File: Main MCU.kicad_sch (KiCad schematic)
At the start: 15 parts, among them J9 Conn_01x06_Pin, SW3 RESET, U1 STM32F407VGTx

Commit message: Your descriptive message here
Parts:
- added R53, R54, R55, R56: 560, Resistor_SMD:R_0603_1608Metric, symbol Device:R_US
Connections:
- net B_PWM: now also U1.44 (PE13); no longer U1.66 (PC9)
- net GND: now also D10.1 (K), D11.1 (K), D12.1 (K), D9.1 (K)
- net G_PWM: now also U1.42 (PE11); no longer U1.26 (PA3)
- net R_PWM: now also U1.40 (PE9); no longer U1.45 (PE14)
- net PA0: now reaches U1.23 (PA0)
- net PA0: now also J8.9 (Pin_9)
- net PA5: now reaches U1.30 (PA5)
- net PA5: now also J8.6 (Pin_6)
- net PA6: now reaches U1.31 (PA6)
- net PA6: now also J8.8 (Pin_8)
- net PB1: now reaches U1.36 (PB1)
- net PB1: now also J8.15 (Pin_15)
- net PD11: now reaches U1.58 (PD11)
- net PD11: now also R53.2
- net PD12: now reaches U1.59 (PD12)
- net PD12: now also R54.2
- net PD13: now reaches U1.60 (PD13)
- net PD13: now also R55.1
- net PD14: now reaches U1.61 (PD14)
- net PD14: now also R56.1
- net PD15: now reaches U1.62 (PD15)
- net PD15: now also J8.17 (Pin_17)
- net PA8: now reaches U1.67 (PA8)
- net PA8: now also J8.4 (Pin_4)
- net PC11: now reaches U1.79 (PC11)
- net PC11: now also J8.18 (Pin_18)
- net PB5: now reaches U1.91 (PB5)
- net PB5: now also J8.7 (Pin_7)
- net PA3: now reaches J8.14 (Pin_14)
- net PA3: now also U1.26 (PA3)
- net PE14: now reaches J8.16 (Pin_16)
- net PE14: now also U1.45 (PE14)
- net PC9: now reaches J8.5 (Pin_5)
- net PC9: now also U1.66 (PC9)
- net at D9.2 (A): now also R54.1
- net at D11.2 (A): now also R56.2
- net at D12.2 (A): now also R53.1
- net at D10.2 (A): now also R55.2
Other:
- moved on the sheet: D10, D11, D12, D9, J8

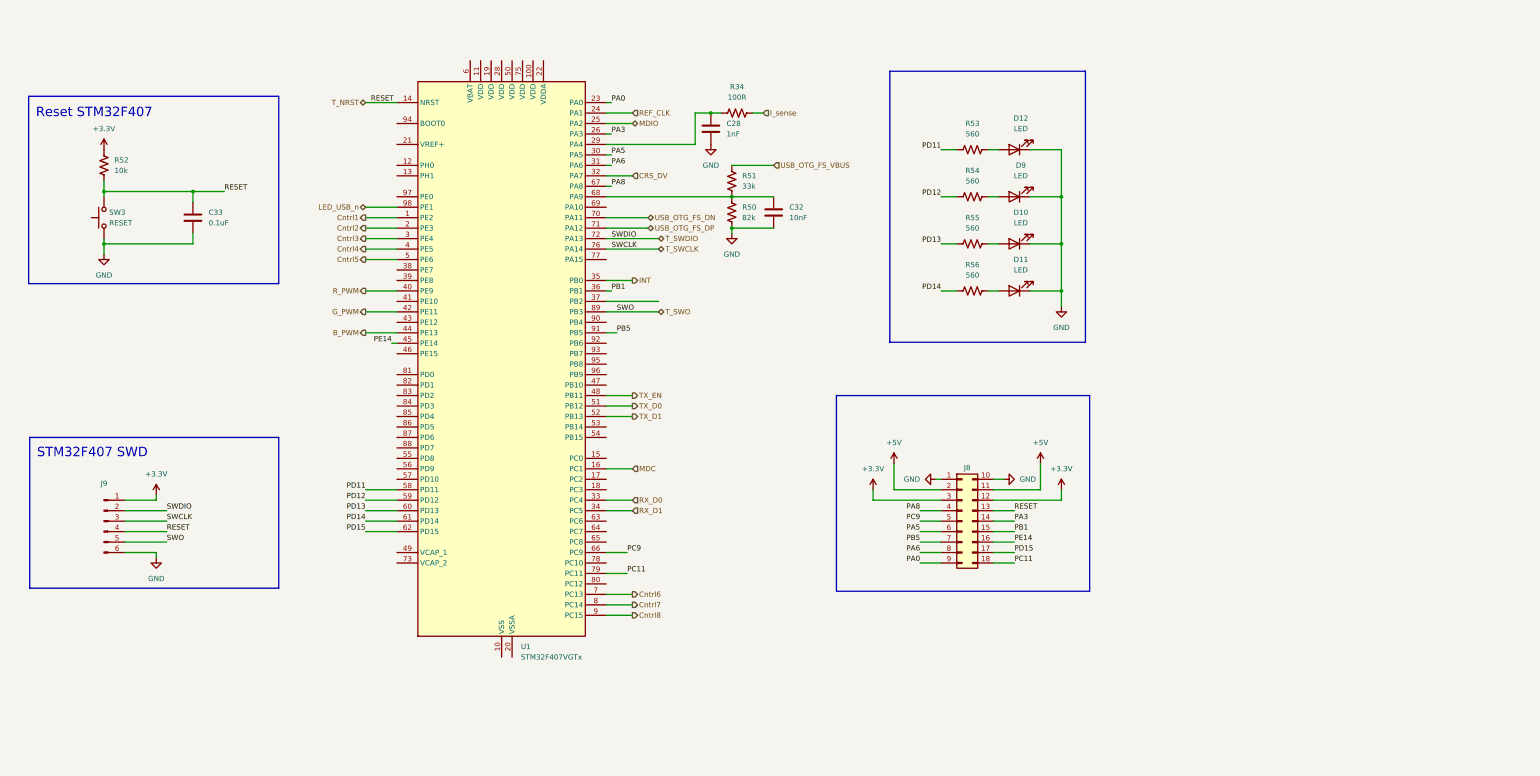
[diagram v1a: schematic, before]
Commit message: Added 3V3 Power Supply
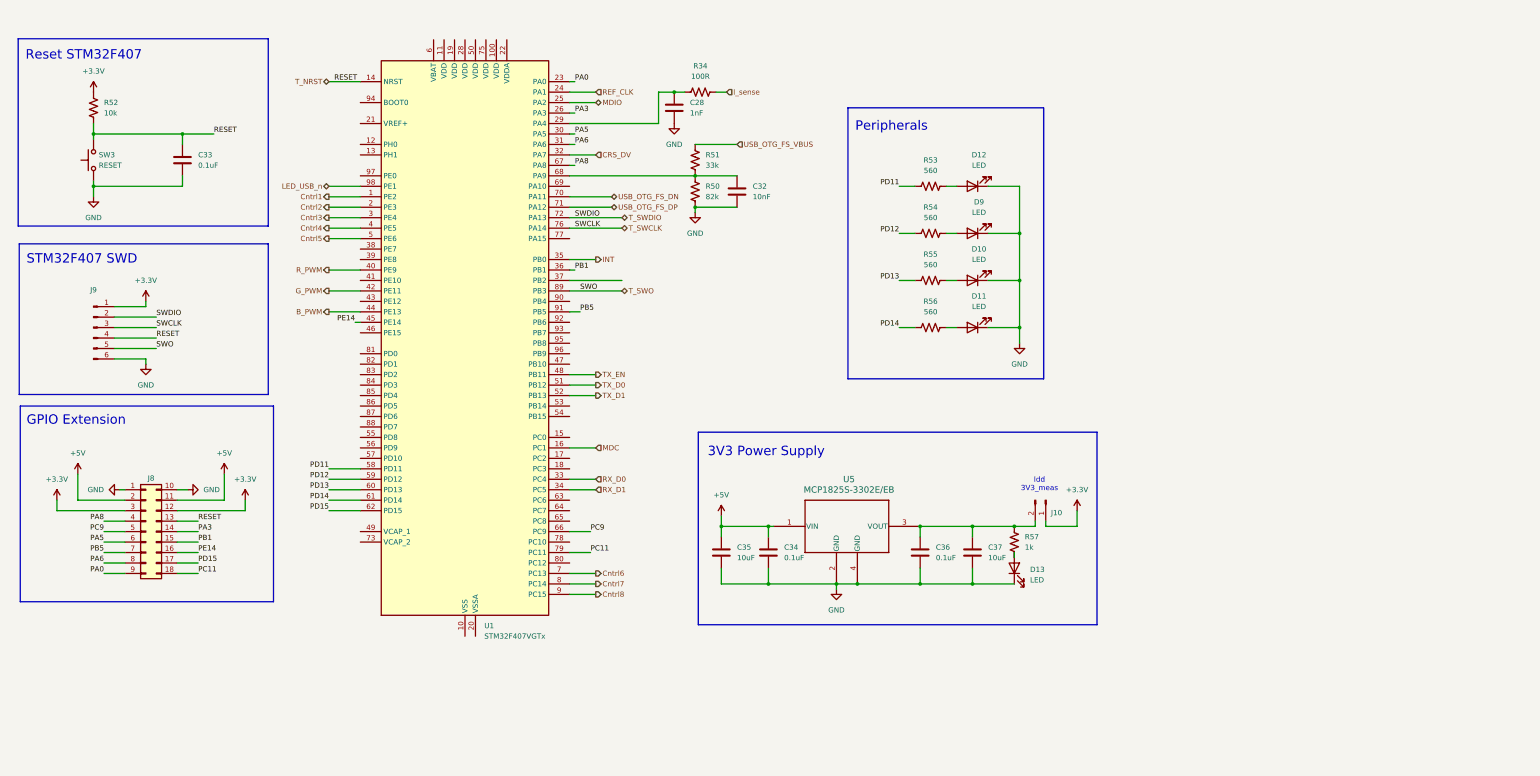
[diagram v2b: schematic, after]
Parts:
- added C34, C36: 0.1uF, Capacitor_SMD:C_0402_1005Metric, symbol Device:C
- added C35, C37: 10uF, Capacitor_SMD:C_0805_2012Metric, symbol Device:C
- added D13: LED, symbol Device:LED
- added J10: Conn_01x02_Pin, Connector_PinHeader_2.54mm:PinHeader_1x02_P2.54mm_Vertical, symbol Connector:Conn_01x02_Pin
- added R57: 1k, Resistor_SMD:R_0603_1608Metric, symbol Device:R_US
- added U5: MCP1825S-3302E/EB, footprints:DDPAK3_MC_MCH-L, symbol MCP1825S-3302EEB:MCP1825S-3302E_EB
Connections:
- net +3.3V: now also J10.1 (Pin_1)
- net +5V: now also C34.1, C35.1, U5.1 (VIN)
- net GND: now also C34.2, C35.2, C36.2, C37.2, D13.1 (K), U5.2 (GND), U5.4 (GND)
- new net: D13.2 (A), R57.2
- new net: C36.1, C37.1, J10.2 (Pin_2), R57.1, U5.3 (VOUT)
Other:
- note added: "3V3 Power Supply"
- note added: "GPIO Extension"
- note added: "Idd 3V3_meas"
- note added: "Peripherals"
- moved on the sheet: C28, C32, C33, D10, D11, D12, D9, J8, J9, R34, R50, R51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

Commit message: MCU power supplied
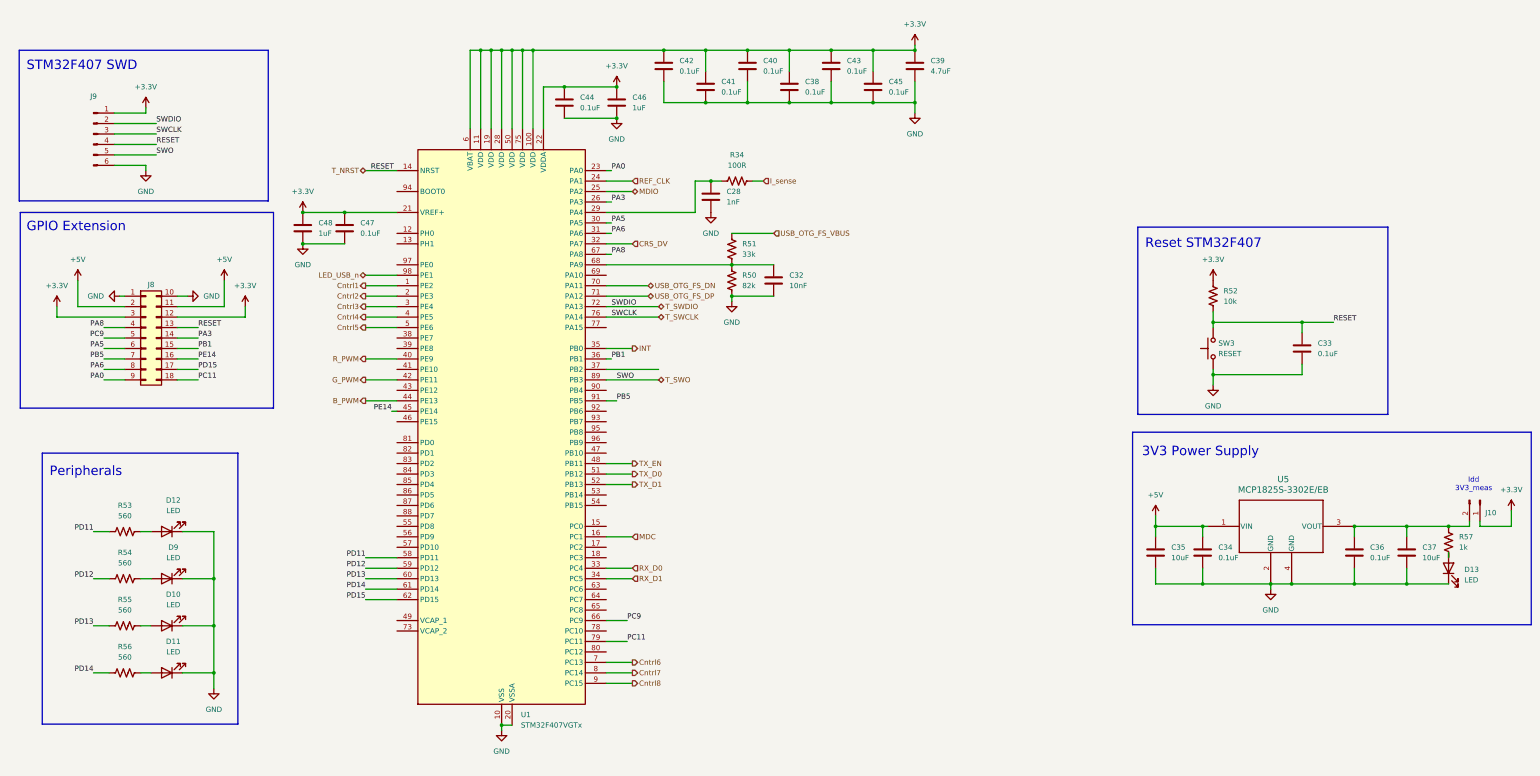
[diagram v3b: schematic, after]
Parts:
- added C38, C40, C41, C42, C43, C44, C45, C47: 0.1uF, Capacitor_SMD:C_0402_1005Metric, symbol Device:C
- added C39: 4.7uF, Capacitor_SMD:C_0805_2012Metric, symbol Device:C
- added C46, C48: 1uF, Capacitor_SMD:C_0603_1608Metric, symbol Device:C
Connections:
- net +3.3V: now also U1.100 (VDD), U1.11 (VDD), U1.19 (VDD), U1.21 (VREF+), U1.22 (VDDA), U1.28 (VDD), U1.50 (VDD), U1.6 (VBAT), U1.75 (VDD), C38.1, C39.1, C40.1, C41.1, C42.1, C43.1, C44.1, C45.1, C46.1, C47.1, C48.1
- net GND: now also U1.10 (VSS), U1.20 (VSSA), U1.27 (VSS), U1.74 (VSS), U1.99 (VSS), C38.2, C39.2, C40.2, C41.2, C42.2, C43.2, C44.2, C45.2, C46.2, C47.2, C48.2
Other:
- moved on the sheet: C28, C32, C33, C34, C35, C36, C37, D10, D11, D12, D13, D9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

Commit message: Added user buttons and boot config
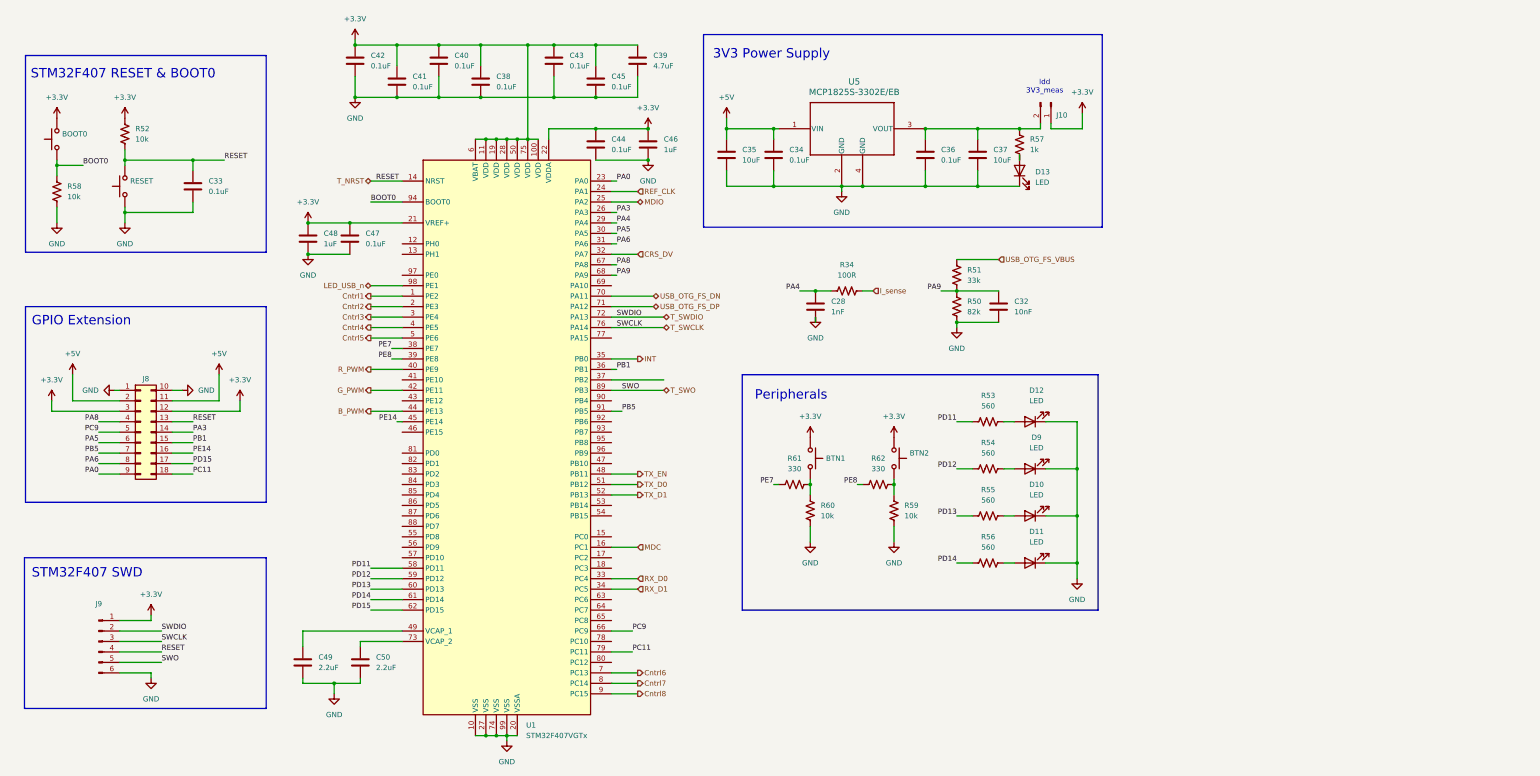
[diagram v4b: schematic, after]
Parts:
- added BOOT0, BTN1, BTN2: ~, Button_Switch_SMD:SW_SPST_PTS645Sx43SMTR92, symbol Switch:SW_Omron_B3FS
- added C49, C50: 2.2uF, Capacitor_SMD:C_0603_1608Metric, symbol Device:C
- added R58, R59, R60: 10k, Resistor_SMD:R_0603_1608Metric, symbol Device:R_US
- added R61, R62: 330, Resistor_SMD:R_0603_1608Metric, symbol Device:R_US
- renumbered SW3 to RESET
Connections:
- net +3.3V: now also BOOT0.2, BTN1.1, BTN2.1
- net GND: now also C49.2, C50.2, R58.2, R59.2, R60.2
- net PA4: now reaches C28.1, R34.1, U1.29 (PA4)
- net PE7: now reaches U1.38 (PE7)
- net PE7: now also R61.1
- net PE8: now reaches U1.39 (PE8)
- net PE8: now also R62.1
- net at U1.49 (VCAP_1): now also C49.1
- net PA9: now reaches C32.1, R50.1, R51.2, U1.68 (PA9)
- net at U1.73 (VCAP_2): now also C50.1
- net BOOT0: now reaches U1.94 (BOOT0)
- net BOOT0: now also BOOT0.1, R58.1
- new net: BTN1.2, R60.1, R61.2
- new net: BTN2.2, R59.1, R62.2
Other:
- note added: "STM32F407 RESET & BOOT0"
- note removed: "Reset STM32F407"
- moved on the sheet: C28, C32, C33, C34, C35, C36, C37, C38, C39, C40, C41, C42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

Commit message: update
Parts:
- C32: footprint Capacitor_SMD:C_0603_1608Metric -> Capacitor_SMD:C_0402_1005Metric; MPN (none) -> GRM155R71E103KA01D; Manufacturer (none) -> Murata Electronics
- D10, D11, D12, D13, D9: footprint (none) -> LED_SMD:LED_0805_2012Metric
- SW3: renamed from BOOT0; value ~ -> SW_Push
- SW4: renamed from BTN1; value ~ -> SW_Push
- SW5: renamed from BTN2; value ~ -> SW_Push
- SW6: renamed from RESET; value RESET -> SW_Push
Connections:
- no-connect marks 0 -> 36
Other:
- note added: "BOOT0"
- note added: "BTN1"
- note added: "BTN2"
- note added: "RESET"
- moved on the sheet: C33, C34, C35, C36, C37, C38, C39, C40, C41, C42, C43, C44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

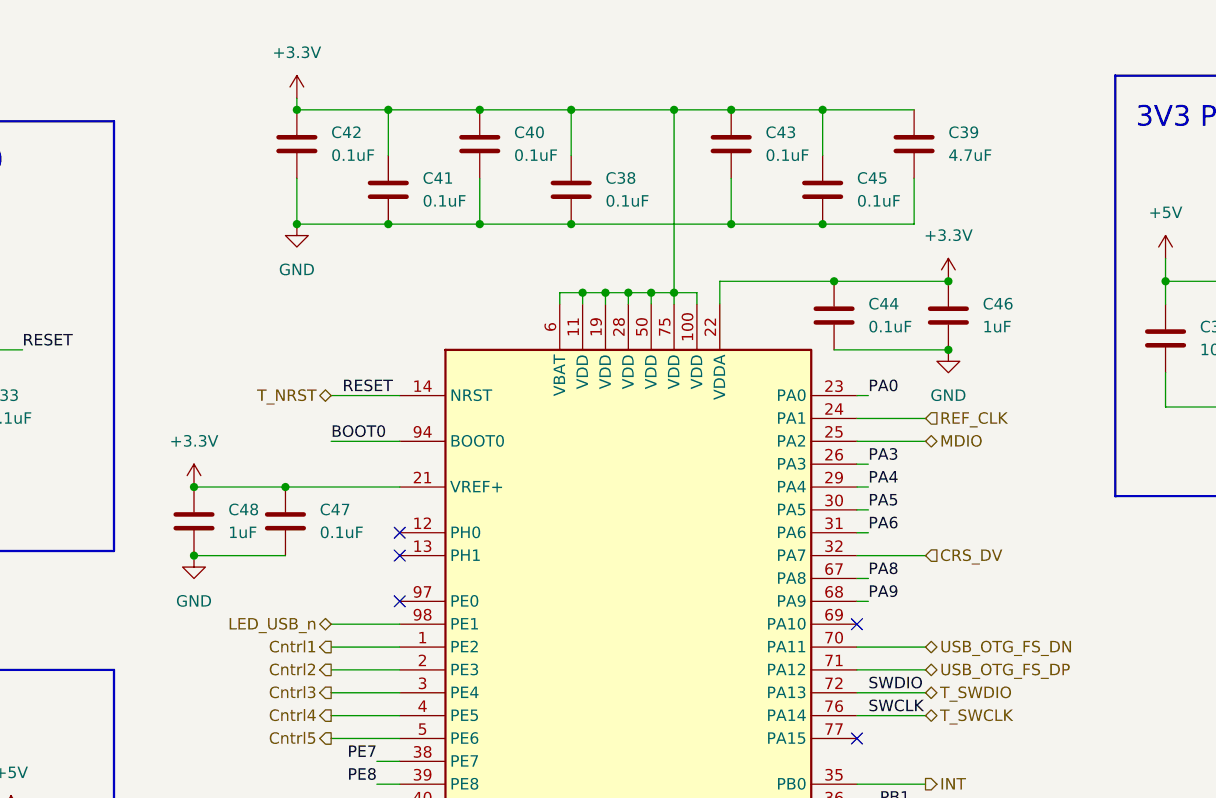
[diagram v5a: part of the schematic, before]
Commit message: Updated the root schematic page
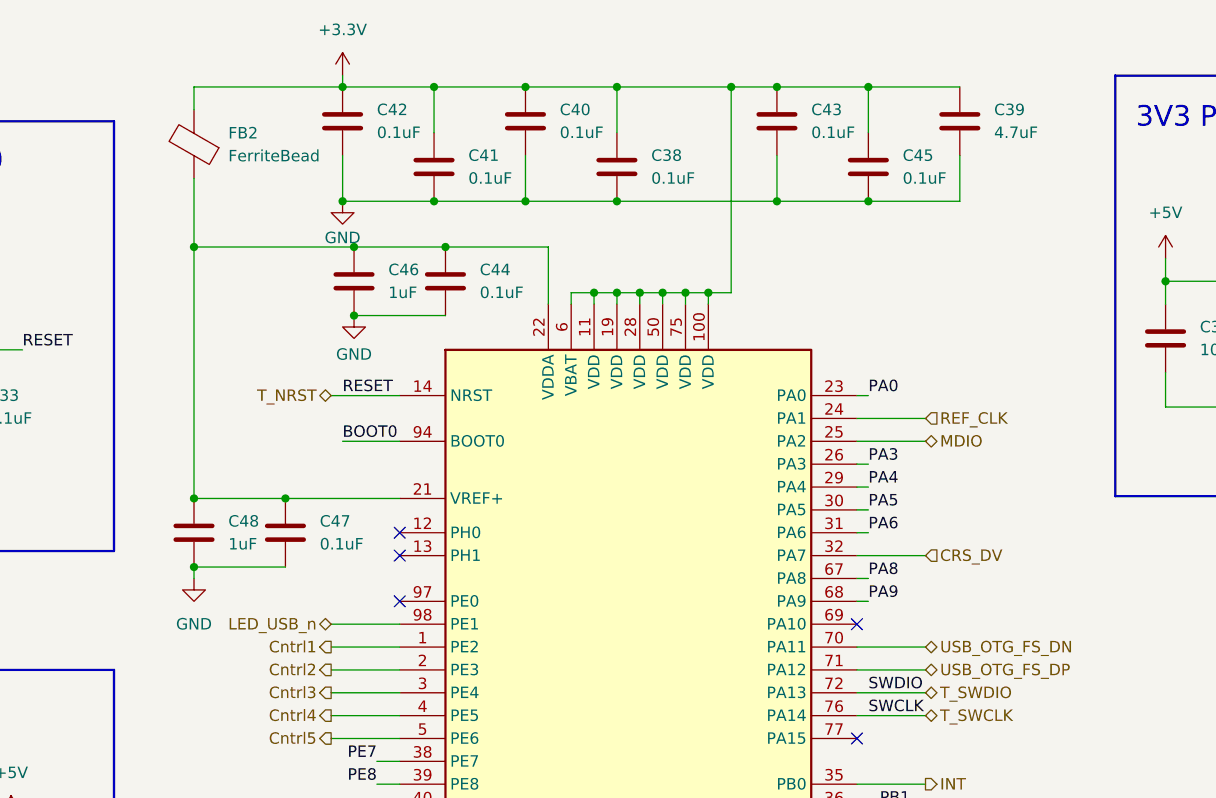
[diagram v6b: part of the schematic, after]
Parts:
- added FB2: FerriteBead, Inductor_SMD:L_0603_1608Metric, symbol Device:FerriteBead
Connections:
- net +3.3V: now also FB2.2; no longer C44.1, C46.1, C47.1, C48.1, U1.21 (VREF+), U1.22 (VDDA)
- new net: C44.1, C46.1, C47.1, C48.1, FB2.1, U1.21 (VREF+), U1.22 (VDDA)
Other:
- moved on the sheet: C38, C39, C40, C41, C42, C43, C44, C45, C46, C47, C48

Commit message: Done ERC + Documentation
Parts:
- U1: MPN (none) -> STM32F407VGTx
- U2: renamed from U5; MPN (none) -> MCP1825S-3302E/EB
- renumbered C33 to C1, C40 to C10, C38 to C11, C43 to C12, C45 to C13, C39 to C14, C35 to C15, C34 to C16, C28 to C17, C36 to C18, C37 to C19, C49 to C2, C32 to C20, C48 to C3, C47 to C4, C50 to C5, C42 to C6, C46 to C7, C41 to C8, C44 to C9, D13 to D1, D12 to D2, D9 to D3, D10 to D4, D11 to D5, FB2 to FB1, J9 to J1, J8 to J2, J10 to J3, R58 to R1, R53 to R10, R54 to R11, R55 to R12, R56 to R13, R57 to R14, R52 to R2, R61 to R3, R60 to R4, R34 to R5, R62 to R6, R59 to R7, R51 to R8, R50 to R9, SW3 to SW1, SW6 to SW2, SW4 to SW3, SW5 to SW4
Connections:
- net T_NRST renamed RESET

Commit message: Initial Review Changes
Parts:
- added TP1: BOOT0, TestPoint:TestPoint_Pad_D1.0mm, symbol Connector:TestPoint
- added TP2: NRST, TestPoint:TestPoint_Pad_D1.0mm, symbol Connector:TestPoint
- added TP3: GND, TestPoint:TestPoint_Keystone_5000-5004_Miniature, symbol Connector:TestPoint
- added TP4: 3V3, TestPoint:TestPoint_Keystone_5000-5004_Miniature, symbol Connector:TestPoint
- J1: value Conn_01x06_Pin -> F407 SWD
- J2: value ~ -> GPIO
- renumbered R14 to R10, R10 to R11, R11 to R12, R12 to R13, R13 to R14
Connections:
- net +3.3V: now also TP4.1
- net BOOT0: now also TP1.1
- net GND: now also TP3.1
- net RESET: now also TP2.1
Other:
- company: (none) -> _electronic_projects
- title: (none) -> DeskNode-F4
- moved on the sheet: C1, C12, C13, C14, C15, C16, C18, C19, D1, J1, J2, J3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
